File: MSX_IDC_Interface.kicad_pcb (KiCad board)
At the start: 2 copper layers, 101.6 x 63.4 mm, 11 parts, among them J1 DE1 GPIO, U1 74LS00, U2 MSX_BUS, U3 74LVC245A, U4 74LVC245A, U5 74LVC245A, U6 74LVC245A, U7 74LVC245A

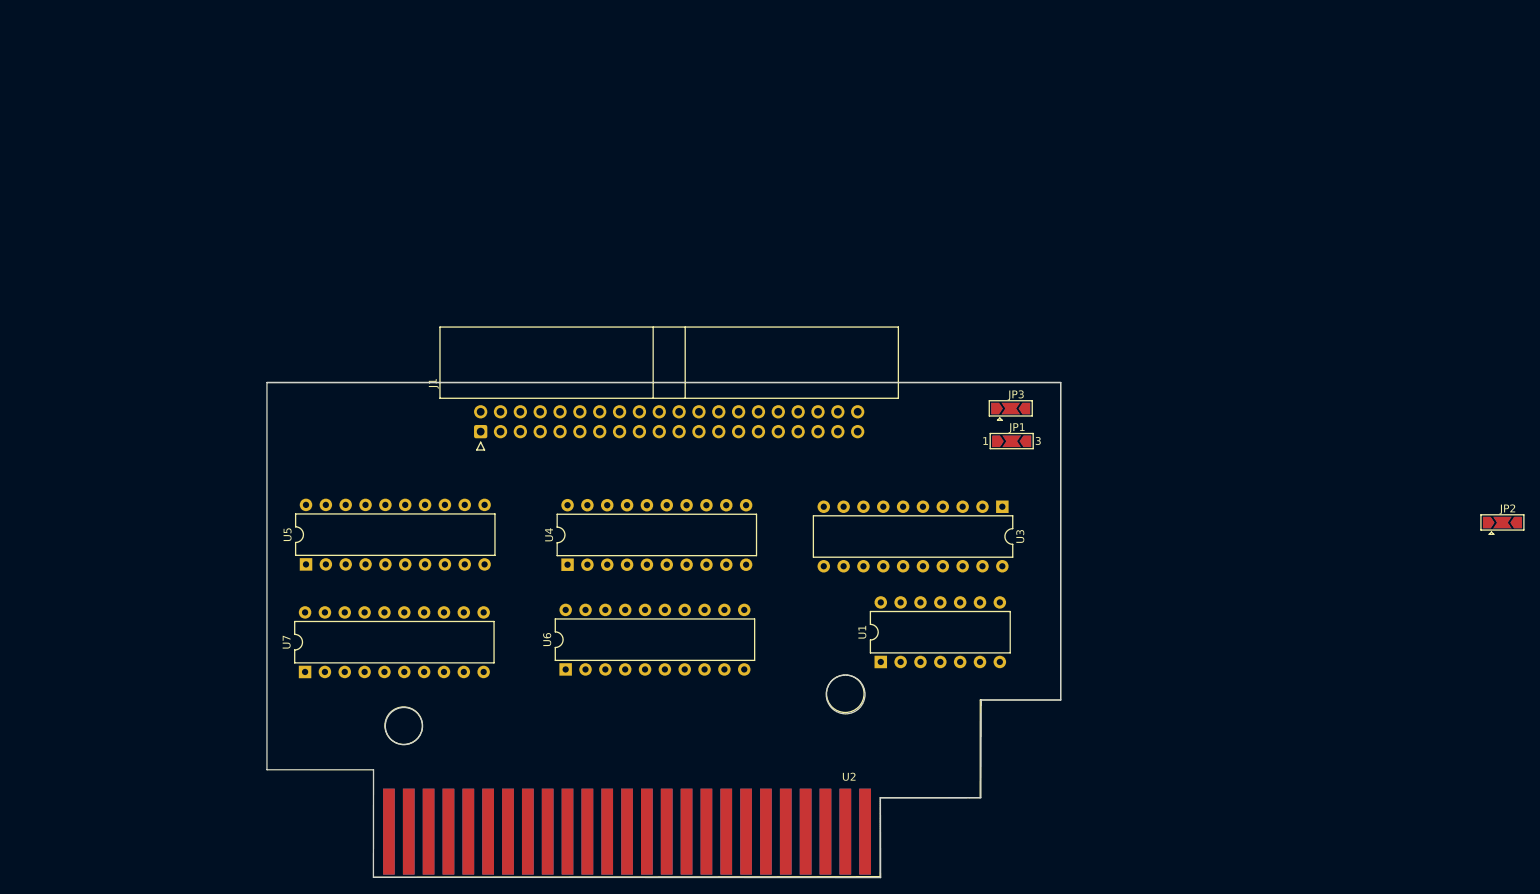
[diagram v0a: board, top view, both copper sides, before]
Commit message: Changed the schematic to use a NAND port via transitors - to remove the 74LS00. Started routing the PCB
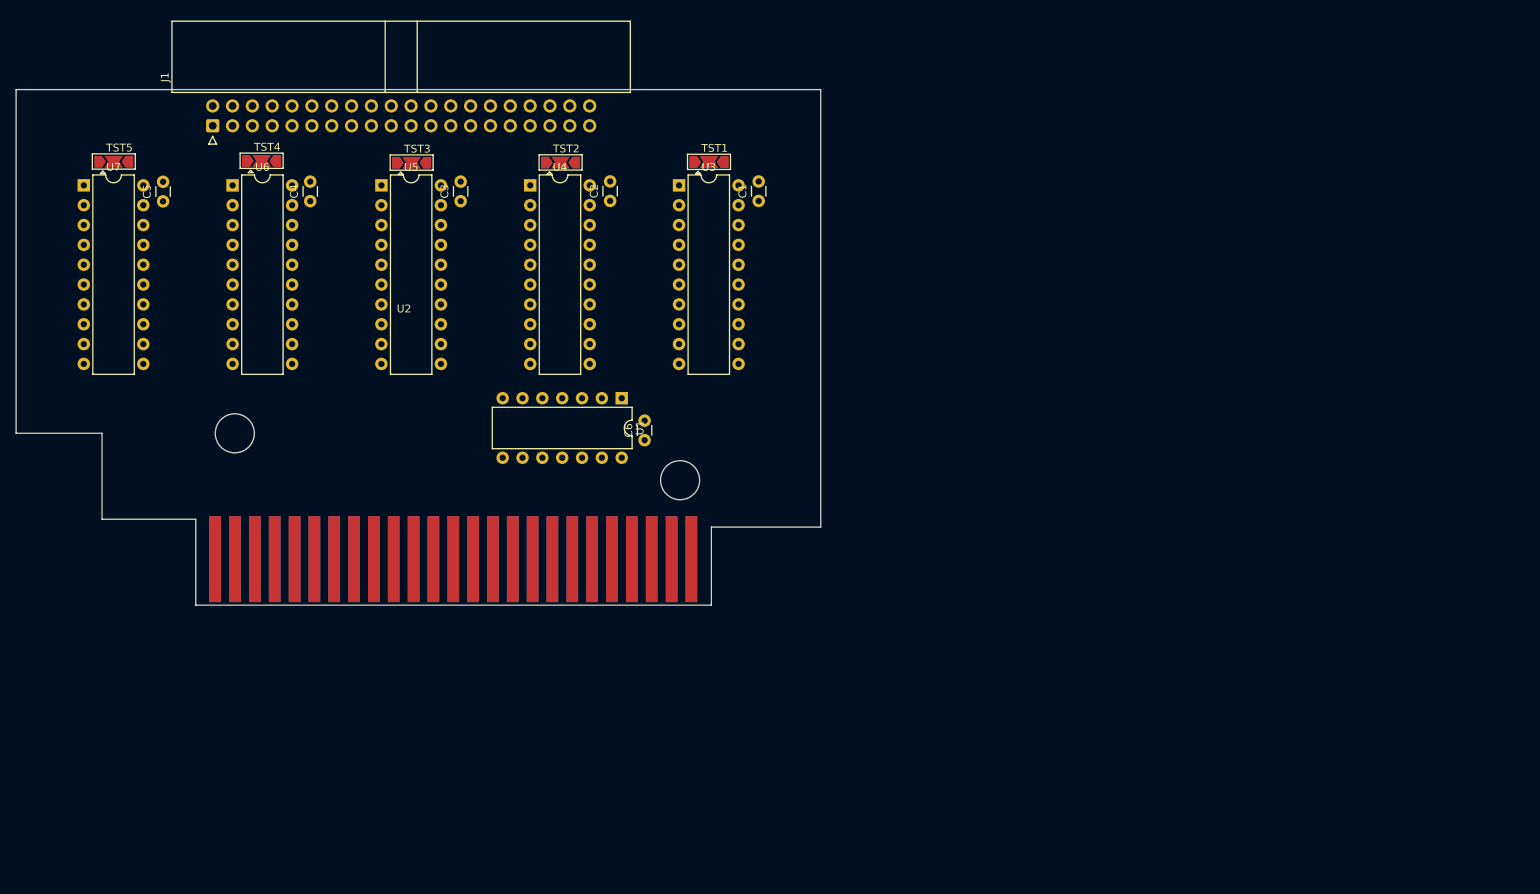
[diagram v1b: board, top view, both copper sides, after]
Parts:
- removed JP1: Jumper_2_Open, Jumper:SolderJumper-3_P2.0mm_Open_TrianglePad1.0x1.5mm_NumberLabels
- removed JP2, JP3: SolderJumper_3_Open, Jumper:SolderJumper-3_P2.0mm_Open_TrianglePad1.0x1.5mm
- added C1: 0.1uf, Capacitor_THT:C_Disc_D3.0mm_W1.6mm_P2.50mm, F.Cu at (133.4, 35.0)
- added C2: 0.1uf, Capacitor_THT:C_Disc_D3.0mm_W1.6mm_P2.50mm, F.Cu at (114.4, 35.0)
- added C3: 0.1uf, Capacitor_THT:C_Disc_D3.0mm_W1.6mm_P2.50mm, F.Cu at (95.2, 35.0)
- added C4: 0.1uf, Capacitor_THT:C_Disc_D3.0mm_W1.6mm_P2.50mm, F.Cu at (76.0, 35.0)
- added C5: 0.1uf, Capacitor_THT:C_Disc_D3.0mm_W1.6mm_P2.50mm, F.Cu at (57.1, 35.1)
- added C6: 0.1uf, Capacitor_THT:C_Disc_D3.0mm_W1.6mm_P2.50mm, F.Cu at (118.8, 65.6)
- added TST1: SolderJumper_3_Open, Jumper:SolderJumper-3_P2.0mm_Open_TrianglePad1.0x1.5mm, F.Cu at (127.0, 30.0)
- added TST2: SolderJumper_3_Open, Jumper:SolderJumper-3_P2.0mm_Open_TrianglePad1.0x1.5mm, F.Cu at (108.0, 30.1)
- added TST3: SolderJumper_3_Open, Jumper:SolderJumper-3_P2.0mm_Open_TrianglePad1.0x1.5mm, F.Cu at (89.0, 30.1)
- added TST4: SolderJumper_3_Open, Jumper:SolderJumper-3_P2.0mm_Open_TrianglePad1.0x1.5mm, F.Cu at (69.8, 29.9)
- added TST5: SolderJumper_3_Open, Jumper:SolderJumper-3_P2.0mm_Open_TrianglePad1.0x1.5mm, F.Cu at (50.8, 30.0)
- moved U6 75.2 mm to (66.0, 33.0), turned to 0 degrees
- moved U2 70.5 mm to (88.0, 51.4)
- moved U7 68.4 mm to (47.0, 33.0), turned to 0 degrees
- moved U3 58.4 mm to (123.2, 33.0), turned to 0 degrees
- moved J1 52.1 mm to (63.5, 25.4)
- moved U5 49.5 mm to (85.1, 33.0), turned to 0 degrees
- moved U4 48.8 mm to (104.2, 33.0), turned to 0 degrees
- moved U1 47.3 mm to (115.9, 60.3), turned to -90 degrees
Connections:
- U3 pad 11: (no net) -> /C_M1
- U3 pad 12: (no net) -> /C_INT
- U3 pad 13: (no net) -> /C_WAIT
- U3 pad 14: (no net) -> /C_RFSH
- U3 pad 15: (no net) -> /C_SLTSL
- U3 pad 16: (no net) -> /C_CS12
- U3 pad 17: (no net) -> /C_CS2
- U4 pad 11: (no net) -> C_SOUNDIN
- U4 pad 12: (no net) -> C_CLOCK
- U4 pad 13: (no net) -> /C_RESET
- U4 pad 14: (no net) -> /C_RD
- U4 pad 15: (no net) -> unconnected-(U4-Pad15)
- U4 pad 16: (no net) -> /C_MREQ
- U4 pad 17: (no net) -> /C_IORQ
- U5 pad 11: (no net) -> C_A8
- U5 pad 12: (no net) -> C_A9
- U5 pad 13: (no net) -> C_A10
- U5 pad 14: (no net) -> C_A11
- U5 pad 15: (no net) -> C_A12
- U5 pad 16: (no net) -> C_A13
- U5 pad 17: (no net) -> C_A14
- U5 pad 19: C_A14 -> Net-(TST3-Pad2)
- U6 pad 11: (no net) -> C_A0
- U6 pad 12: (no net) -> C_A1
- U6 pad 13: (no net) -> C_A2
- U6 pad 14: (no net) -> C_A3
- U6 pad 15: (no net) -> C_A4
- U6 pad 16: (no net) -> C_A5
- U6 pad 17: (no net) -> C_A6
- U6 pad 19: C_A6 -> Net-(TST4-Pad2)
- U7 pad 11: (no net) -> C_D0
- U7 pad 12: (no net) -> C_D1
- U7 pad 13: (no net) -> C_D2
- U7 pad 14: (no net) -> C_D3
- U7 pad 15: (no net) -> C_D4
- U7 pad 16: (no net) -> C_D5
- U7 pad 17: (no net) -> C_D6
- U7 pad 19: C_D6 -> Net-(TST5-Pad2)
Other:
- board size 101.6 x 63.4 mm -> 103 x 66 mm

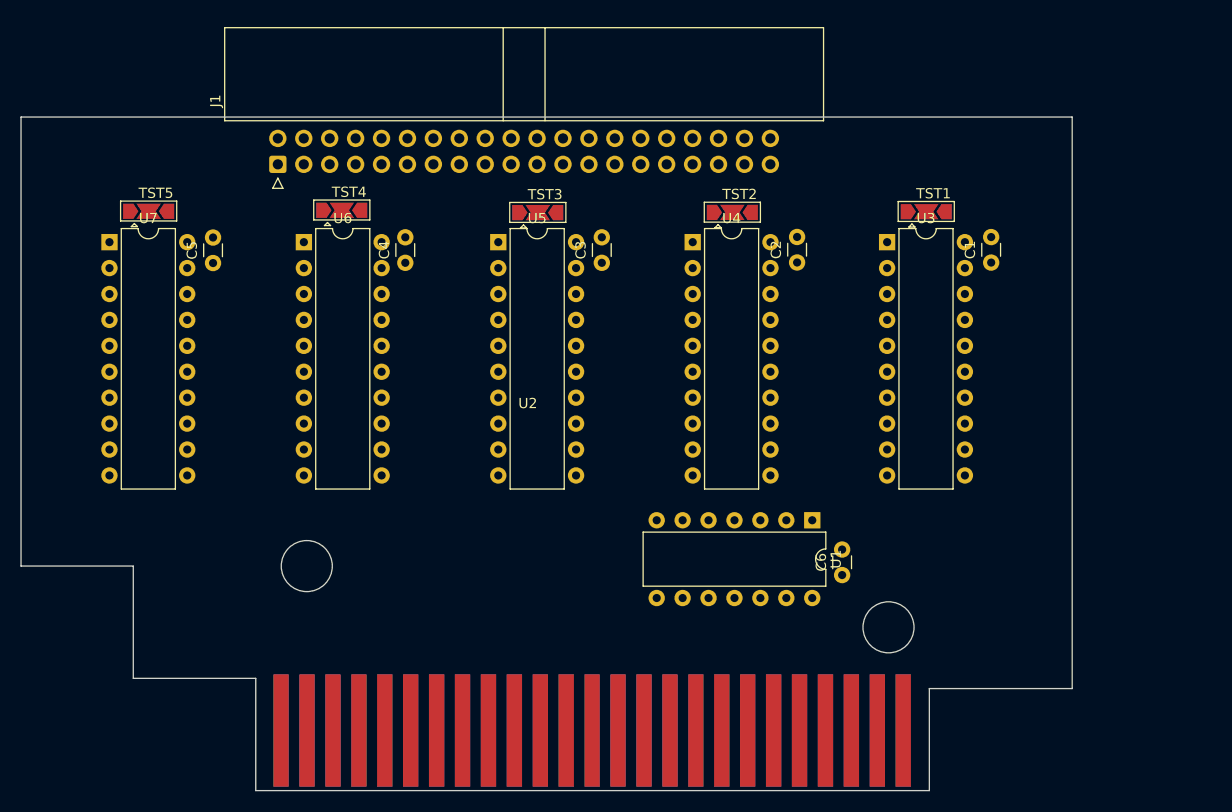
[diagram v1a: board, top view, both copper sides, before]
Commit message: Added both NAD options to same schematic -with 74LS00 and other option with tranistors
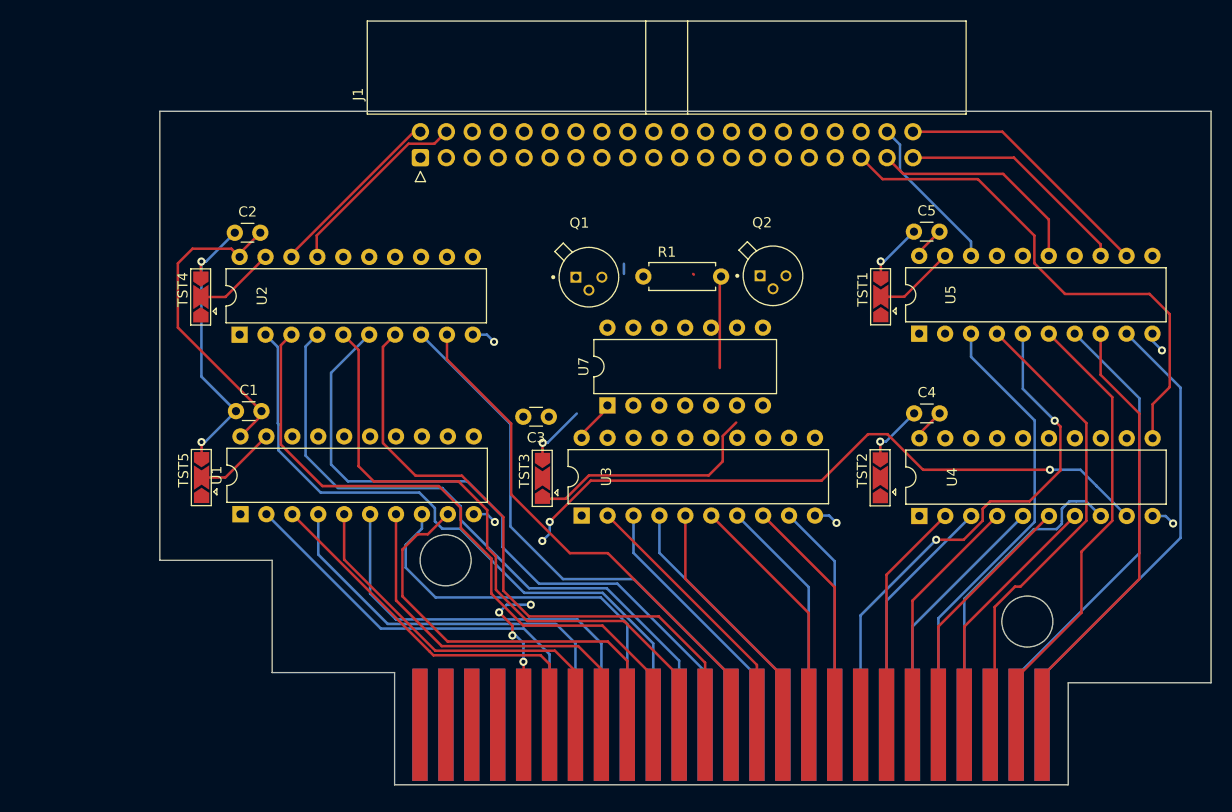
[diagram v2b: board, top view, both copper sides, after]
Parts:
- removed C6: 0.1uf, Capacitor_THT:C_Disc_D3.0mm_W1.6mm_P2.50mm
- removed U6: 74LVC245A, Package_DIP:DIP-20_W7.62mm
- added CONN1: MSX_BUS, Roni Footprints:MSX_CART, F.Cu at (101.6, 50.8)
- added Q1: 2N2222, Roni Footprints:TO127P584H533-3, F.Cu at (94.0, 36.5)
- added Q2: 2N2222, Roni Footprints:TO127P584H533-3, F.Cu at (112.0, 36.3)
- added R1: 1k, Resistor_THT:R_Axial_DIN0207_L6.3mm_D2.5mm_P7.62mm_Horizontal, F.Cu at (99.3, 36.4)
- U1: value 74LS00 -> 74LVC245A; footprint Package_DIP:DIP-14_W7.62mm -> Package_DIP:DIP-20_W7.62mm
- U2: value MSX_BUS -> 74LVC245A; footprint Roni Footprints:MSX_CART -> Package_DIP:DIP-20_W7.62mm
- U7: value 74LVC245A -> 74LS00; footprint Package_DIP:DIP-20_W7.62mm -> Package_DIP:DIP-14_W7.62mm
- moved C1 75.4 mm to (59.4, 49.6), turned to 0 degrees
- moved C5 68.7 mm to (125.8, 32.0), turned to 0 degrees
- moved U1 56.0 mm to (59.8, 59.7), turned to 90 degrees
- moved C2 55.2 mm to (59.3, 32.1), turned to 0 degrees
- moved C4 52.0 mm to (125.8, 49.8), turned to 0 degrees
- moved U7 51.3 mm to (95.8, 49.0), turned to 90 degrees
- moved U5 42.2 mm to (126.3, 42.0), turned to 90 degrees
- moved U3 40.2 mm to (93.3, 59.8), turned to 90 degrees
- moved U4 34.8 mm to (126.4, 59.9), turned to 90 degrees
- moved TST2 29.8 mm to (122.5, 56.1), turned to 90 degrees
- moved U2 29.7 mm to (59.8, 42.1), turned to 90 degrees
- moved TST5 26.6 mm to (56.0, 56.1), turned to 90 degrees
- moved TST3 26.0 mm to (89.4, 56.2), turned to 90 degrees
- moved TST4 16.2 mm to (56.0, 38.4), turned to 90 degrees
- moved C3 16.0 mm to (90.1, 50.1), turned to 180 degrees
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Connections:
- J1 pad 1: /C_CS1 -> C_D7
- J1 pad 10: /C_IORQ -> C_A1
- J1 pad 13: C_A12 -> C_D2
- J1 pad 14: /C_MREQ -> C_A0
- J1 pad 15: C_A11 -> C_D1
- J1 pad 16: /C_WR -> C_A14
- J1 pad 17: C_A10 -> C_D0
- J1 pad 18: /C_RD -> C_A13
- J1 pad 19: C_A9 -> /C_BUSDIR
- J1 pad 2: /C_CS1 -> C_A5
- J1 pad 20: /C_RESET -> C_A8
- J1 pad 21: C_A8 -> /C_IORQ
- J1 pad 22: C_CLOCK -> C_A12
- J1 pad 23: C_A7 -> /C_MREQ
- J1 pad 24: C_D7 -> C_A7
- J1 pad 25: C_A6 -> /C_WR
- J1 pad 26: C_D6 -> C_A6
- J1 pad 27: C_A5 -> /C_RD
- J1 pad 28: C_D5 -> C_A10
- J1 pad 3: /C_CS12 -> C_D6
- J1 pad 31: C_A4 -> /C_RESET
- J1 pad 32: C_D4 -> C_A11
- J1 pad 33: C_A3 -> C_CLOCK
- J1 pad 34: C_D3 -> C_A15
- J1 pad 35: C_A2 -> C_SOUNDIN
- J1 pad 36: C_D2 -> C_A9
- J1 pad 37: C_A1 -> /C_SLTSL
- J1 pad 38: C_D1 -> /C_CS1
- J1 pad 39: C_A0 -> /C_WAIT
- J1 pad 4: /C_SLTSL -> C_A4
- J1 pad 40: C_D0 -> /C_INT
- J1 pad 5: C_A15 -> C_D5
- J1 pad 6: /C_WAIT -> C_A3
- J1 pad 7: C_A14 -> C_D4
- J1 pad 8: /C_BUSDIR -> C_A2
- J1 pad 9: C_A13 -> C_D3
- TST1 pad 1: Net-(TST1-Pad1) -> Net-(Q2-Pad3)
- TST2 pad 1: Net-(TST1-Pad1) -> Net-(Q2-Pad3)
- TST3 pad 1: Net-(TST1-Pad1) -> Net-(Q2-Pad3)
- TST4 pad 1: Net-(TST1-Pad1) -> Net-(Q2-Pad3)
- TST5 pad 1: Net-(TST1-Pad1) -> Net-(Q2-Pad3)
- U1 pad 1: Net-(U1-Pad1) -> unconnected-(U1-Pad1)
- U1 pad 10: unconnected-(U1-Pad10) -> GNDREF
- U1 pad 11: unconnected-(U1-Pad11) -> C_D0
- U1 pad 12: unconnected-(U1-Pad12) -> C_D1
- U1 pad 13: unconnected-(U1-Pad13) -> C_D2
- U1 pad 14: +5V -> C_D3
- U1 pad 2: Net-(U1-Pad2) -> D7
- U1 pad 3: Net-(TST1-Pad1) -> D6
- U1 pad 4: unconnected-(U1-Pad4) -> D5
- U1 pad 5: unconnected-(U1-Pad5) -> D4
- U1 pad 6: unconnected-(U1-Pad6) -> D3
- U1 pad 7: GNDREF -> D2
- U1 pad 8: unconnected-(U1-Pad8) -> D1
- U1 pad 9: unconnected-(U1-Pad9) -> D0
- U2 pad 1: Net-(U2-Pad1) -> unconnected-(U2-Pad1)
- U2 pad 10: Net-(U2-Pad10) -> GNDREF
- U2 pad 11: Net-(U2-Pad11) -> C_A13
- U2 pad 12: Net-(U2-Pad12) -> C_A14
- U2 pad 13: Net-(U1-Pad1) -> C_A0
- U2 pad 14: Net-(U1-Pad2) -> C_A1
- U2 pad 15: Net-(U2-Pad15) -> C_A2
- U2 pad 16: unconnected-(U2-Pad16) -> C_A3
- U2 pad 17: Net-(U2-Pad17) -> C_A4
- U2 pad 18: Net-(U2-Pad18) -> C_A5
- U2 pad 19: Net-(U2-Pad19) -> Net-(TST4-Pad2)
- U2 pad 2: Net-(U2-Pad2) -> A5
- U2 pad 20: Net-(U2-Pad20) -> +3.3V
- U2 pad 3: Net-(U2-Pad3) -> A4
- U2 pad 4: Net-(U2-Pad4) -> A3
- U2 pad 5: unconnected-(U2-Pad5) -> A2
- U2 pad 6: Net-(U2-Pad6) -> A1
- U2 pad 7: Net-(U2-Pad7) -> A0
- U2 pad 8: Net-(U2-Pad8) -> A14
- U2 pad 9: Net-(U2-Pad9) -> A13
- U3 pad 1: Net-(U1-Pad2) -> unconnected-(U3-Pad1)
- U3 pad 11: /C_M1 -> C_A9
- U3 pad 12: /C_INT -> C_A15
- U3 pad 13: /C_WAIT -> C_A11
- U3 pad 14: /C_RFSH -> C_A10
- U3 pad 15: /C_SLTSL -> C_A6
- U3 pad 16: /C_CS12 -> C_A7
- U3 pad 17: /C_CS2 -> C_A12
- U3 pad 18: /C_CS1 -> C_A8
- U3 pad 19: Net-(TST1-Pad2) -> Net-(TST3-Pad2)
- U3 pad 2: Net-(U2-Pad1) -> A8
- U3 pad 3: Net-(U2-Pad2) -> A12
- U3 pad 4: Net-(U2-Pad3) -> A7
- U3 pad 5: Net-(U2-Pad4) -> A6
- U3 pad 6: Net-(U2-Pad6) -> A10
- U3 pad 7: Net-(U2-Pad7) -> A11
- U3 pad 8: Net-(U2-Pad8) -> A15
- U3 pad 9: Net-(U2-Pad9) -> A9
- U4 pad 1: Net-(U1-Pad2) -> unconnected-(U4-Pad1)
- U4 pad 11: C_SOUNDIN -> C_CLOCK
- U4 pad 12: C_CLOCK -> /C_WAIT
- U4 pad 13: /C_RESET -> /C_INT
- U4 pad 14: /C_RD -> /C_BUSDIR
- U4 pad 15: unconnected-(U4-Pad15) -> /C_IORQ
- U4 pad 17: /C_IORQ -> /C_WR
- U4 pad 18: /C_BUSDIR -> /C_RD
- U4 pad 2: Net-(U2-Pad10) -> /RD
- U4 pad 3: Net-(U2-Pad11) -> /WR
- U4 pad 4: Net-(U2-Pad12) -> /MREQ
- U4 pad 5: Net-(U1-Pad1) -> /IORQ
- U4 pad 6: Net-(U1-Pad2) -> /BUSDIR
- U4 pad 7: Net-(U2-Pad15) -> /INT
- U4 pad 8: Net-(U2-Pad42) -> /WAIT
- U4 pad 9: Net-(U2-Pad49) -> /RESET
- U5 pad 1: Net-(U1-Pad2) -> unconnected-(U5-Pad1)
- U5 pad 11: C_A8 -> /C_CS1
- U5 pad 12: C_A9 -> /C_CS2
- U5 pad 13: C_A10 -> /C_CS12
- U5 pad 14: C_A11 -> /C_SLTSL
- U5 pad 15: C_A12 -> /C_RESET
- U5 pad 16: C_A13 -> /C_RFSH
- U5 pad 17: C_A14 -> /C_M1
- U5 pad 18: C_A15 -> C_SOUNDIN
- U5 pad 19: Net-(TST3-Pad2) -> Net-(TST1-Pad2)
- U5 pad 2: Net-(U2-Pad18) -> SOUNDIN
- U5 pad 3: Net-(U2-Pad25) -> /M1
- U5 pad 4: Net-(U2-Pad26) -> /RFSH
- U5 pad 5: Net-(U2-Pad23) -> CLOCK
- U5 pad 6: Net-(U2-Pad19) -> /SLTSL
- U5 pad 7: Net-(U2-Pad20) -> /CS12
- U5 pad 8: Net-(U2-Pad17) -> /CS2
- U5 pad 9: Net-(U2-Pad24) -> /CS1
- U7 pad 1: Net-(U1-Pad2) -> /WR
- U7 pad 10: GNDREF -> unconnected-(U7-Pad10)
- U7 pad 11: C_D0 -> unconnected-(U7-Pad11)
- U7 pad 12: C_D1 -> unconnected-(U7-Pad12)
- U7 pad 13: C_D2 -> unconnected-(U7-Pad13)
- U7 pad 14: C_D3 -> +3.3V
- U7 pad 2: Net-(U2-Pad39) -> /RD
- U7 pad 3: Net-(U2-Pad40) -> Net-(Q2-Pad3)
- U7 pad 4: Net-(U2-Pad37) -> unconnected-(U7-Pad4)
- U7 pad 5: Net-(U2-Pad38) -> unconnected-(U7-Pad5)
- U7 pad 6: Net-(U2-Pad35) -> unconnected-(U7-Pad6)
- U7 pad 7: Net-(U2-Pad36) -> GNDREF
- U7 pad 8: Net-(U2-Pad33) -> unconnected-(U7-Pad8)
- U7 pad 9: Net-(U2-Pad34) -> unconnected-(U7-Pad9)
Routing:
- net CLOCK: track 0.00 -> 67.4 mm, vias 0 -> 6
- net A1: track 0.00 -> 66.3 mm
- net /RESET: track 0.00 -> 65.7 mm, vias 0 -> 3
- net A5: track 0.00 -> 65.1 mm
- net A4: track 0.00 -> 65.0 mm
- net A3: track 0.00 -> 64.3 mm
- net A2: track 0.00 -> 62.3 mm
- net A0: track 0.00 -> 61.9 mm
- net GNDREF: track 0.00 -> 58.6 mm, vias 0 -> 10
- net A14: track 0.00 -> 54.9 mm
- net A13: track 0.00 -> 51.9 mm
- net C_CLOCK: track 0.00 -> 51.0 mm
- net /RFSH: track 0.00 -> 46.2 mm
- net /CS1: track 0.00 -> 46.1 mm
- net /CS12: track 0.00 -> 46.0 mm
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
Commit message: Safe guard commit - progressing with routing
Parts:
- removed U7: 74LS00, Package_DIP:DIP-14_W7.62mm
- added R2: 1k, Resistor_THT:R_Axial_DIN0207_L6.3mm_D2.5mm_P7.62mm_Horizontal, F.Cu at (64.8, 62.4)
- added R3: 1k, Resistor_THT:R_Axial_DIN0207_L6.3mm_D2.5mm_P7.62mm_Horizontal, F.Cu at (133.5, 62.8)
- added R4: 1k, Resistor_THT:R_Axial_DIN0207_L6.3mm_D2.5mm_P7.62mm_Horizontal, F.Cu at (101.0, 62.6)
- added R5: 1k, Resistor_THT:R_Axial_DIN0207_L6.3mm_D2.5mm_P7.62mm_Horizontal, F.Cu at (133.5, 44.8)
- added R6: 1k, Resistor_THT:R_Axial_DIN0207_L6.3mm_D2.5mm_P7.62mm_Horizontal, F.Cu at (65.2, 44.9)
- added U6: 74LS00, Package_DIP:DIP-14_W7.62mm, F.Cu at (95.7, 48.9)
- moved R1 7.53 mm to (106.8, 36.4), turned to 180 degrees
- moved CONN1 0.30 mm to (101.8, 51.0)
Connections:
- J1 pad 11: +5V -> unconnected-(J1-Pad11)
- J1 pad 19: /C_BUSDIR -> C_A12
- J1 pad 21: /C_IORQ -> C_A7
- J1 pad 22: C_A12 -> C_A6
- J1 pad 23: /C_MREQ -> C_A10
- J1 pad 24: C_A7 -> C_A11
- J1 pad 25: /C_WR -> C_A15
- J1 pad 26: C_A6 -> C_A9
- J1 pad 28: C_A10 -> /C_WR
- J1 pad 29: +3.3V -> unconnected-(J1-Pad29)
- J1 pad 31: /C_RESET -> /C_MREQ
- J1 pad 32: C_A11 -> /C_IORQ
- J1 pad 33: C_CLOCK -> /C_SLTSL
- J1 pad 34: C_A15 -> /C_CS1
- J1 pad 35: C_SOUNDIN -> /C_CS2
- J1 pad 36: C_A9 -> /BUSDIR
- J1 pad 37: /C_SLTSL -> /C_M1
- J1 pad 38: /C_CS1 -> /INT
- J1 pad 39: /C_WAIT -> C_CLOCK
- J1 pad 40: /C_INT -> /WAIT
- R1 pad 2: Net-(Q2-Pad3) -> Net-(R1-Pad2)
- U1 pad 1: unconnected-(U1-Pad1) -> /RD
- U2 pad 1: unconnected-(U2-Pad1) -> Net-(R1-Pad2)
- U3 pad 1: unconnected-(U3-Pad1) -> Net-(R4-Pad2)
- U4 pad 1: unconnected-(U4-Pad1) -> Net-(R3-Pad2)
- U4 pad 11: C_CLOCK -> /C_M1
- U4 pad 12: /C_WAIT -> /C_CS2
- U4 pad 13: /C_INT -> /C_CS1
- U4 pad 14: /C_BUSDIR -> /C_SLTSL
- U4 pad 6: /BUSDIR -> /SLTSL
- U4 pad 7: /INT -> /CS1
- U4 pad 8: /WAIT -> /CS2
- U4 pad 9: /RESET -> /M1
- U5 pad 1: unconnected-(U5-Pad1) -> Net-(R5-Pad2)
- U5 pad 11: /C_CS1 -> unconnected-(U5-Pad11)
- U5 pad 12: /C_CS2 -> unconnected-(U5-Pad12)
- U5 pad 13: /C_CS12 -> unconnected-(U5-Pad13)
- U5 pad 14: /C_SLTSL -> unconnected-(U5-Pad14)
- U5 pad 15: /C_RESET -> C_CLOCK
- U5 pad 17: /C_M1 -> /C_RESET
- U5 pad 18: C_SOUNDIN -> /C_CS12
- U5 pad 2: SOUNDIN -> /CS12
- U5 pad 3: /M1 -> /RESET
- U5 pad 6: /SLTSL -> unconnected-(U5-Pad6)
- U5 pad 7: /CS12 -> unconnected-(U5-Pad7)
- U5 pad 8: /CS2 -> unconnected-(U5-Pad8)
- U5 pad 9: /CS1 -> unconnected-(U5-Pad9)
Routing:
- net GNDREF: track 58.6 -> 167.9 mm, vias 10 -> 8
- net +3.3V: track 37.8 -> 124.3 mm, vias 0 -> 1
- net /RD: track 22.8 -> 93.5 mm, vias 0 -> 1
- net CLOCK: track 67.4 -> 0.00 mm, vias 6 -> 0
- net C_CLOCK: track 51.0 -> 0.00 mm
- net Net-(R1-Pad2): track 0.00 -> 43.1 mm
- net C_D0: track 0.00 -> 40.4 mm
- net /INT: track 24.9 -> 63.6 mm
- net C_A12: track 0.00 -> 38.2 mm
- net /BUSDIR: track 24.9 -> 62.9 mm
- net C_A11: track 0.00 -> 35.4 mm
- net /WAIT: track 31.6 -> 66.6 mm
- net C_D2: track 0.00 -> 34.5 mm, vias 0 -> 1
- net C_D1: track 0.00 -> 33.6 mm, vias 0 -> 1
- net C_A9: track 0.00 -> 33.4 mm
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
